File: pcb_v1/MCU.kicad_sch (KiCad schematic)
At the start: 3 parts, among them U4 ESP32-S3-MINI-1, U6 STM32F103RETx

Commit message: Updated wiring
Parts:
- C12: footprint Capacitor_SMD:C_0805_2012Metric -> Murata Capacitor:CAPC1608X90N
- U4: footprint RF_Module:ESP32-S2-MINI-1 -> ESP32-S3-MINI-1-N8:XCVR_ESP32-S3-MINI-1-N8
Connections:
- net +3.3V: now also U4.3 (3V3)
- net D+: now also U6.45 (PA12)
- net D-: now also U6.44 (PA11)
- net GND: now also U4.1 (GND), U4.2 (GND), U4.42 (GND), U4.43 (GND), U4.46 (GND), U4.47 (GND), U4.48 (GND), U4.49 (GND), U4.50 (GND), U4.51 (GND), U4.52 (GND), U4.53 (GND), U4.54 (GND), U4.55 (GND), U4.56 (GND), U4.57 (GND), U4.58 (GND), U4.59 (GND), U4.60 (GND), U4.61 (GND), U4.62 (GND), U4.63 (GND), U4.64 (GND), U4.65 (GND)
- net SCL: now also U6.58 (PB6)
- net SDA: now also U6.59 (PB7)
- net TXRX: now reaches U6.42 (PA9)
- net TXRX: now also U4.40 (RXD0)
- net RXTX: now reaches U6.43 (PA10)
- net RXTX: now also U4.39 (TXD0)
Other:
- moved on the sheet: C12, U4, U6

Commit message: Update Wiring
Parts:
- removed C12: 100nF, Murata Capacitor:CAPC1608X90N, symbol Device:C
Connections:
- net Column11: now also U6.54 (PD2)
- net Column12: now also U6.55 (PB3)
- net Column13: now also U6.56 (PB4)
- net Column14: now also U6.57 (PB5)
- net Column3: now also U6.25 (PC5)
- net Column4: now also U6.26 (PB0)
- net Column5: now also U6.27 (PB1)
- net Column6: now also U6.28 (PB2)
- net Column7: now also U6.29 (PB10)
- net Column8: now also U6.30 (PB11)
- net RDY: now also U6.61 (PB8)
- net NRST: now reaches U6.7 (NRST)

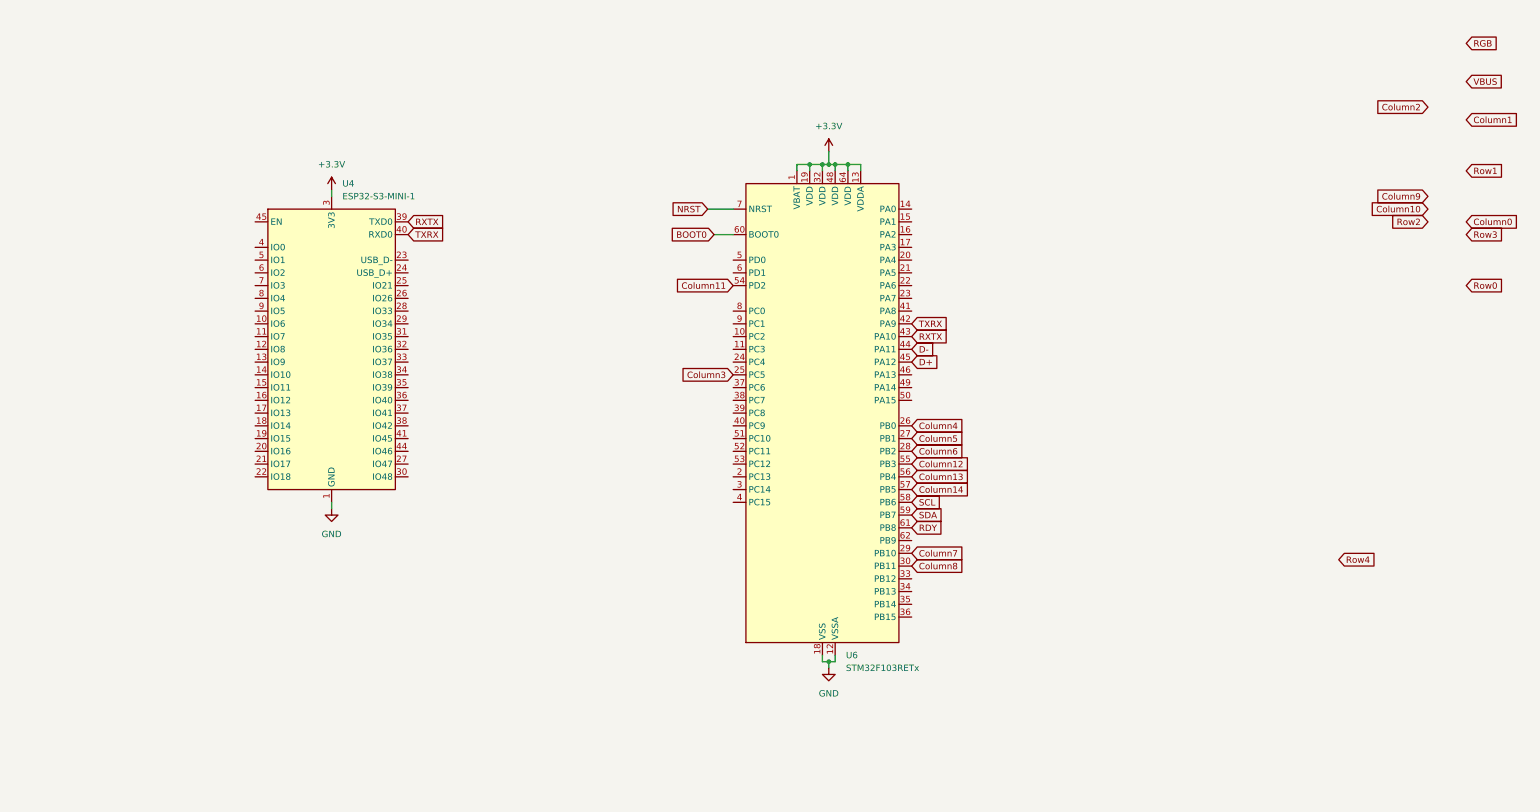
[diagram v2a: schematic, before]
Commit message: Wired all keyboard matrix pins
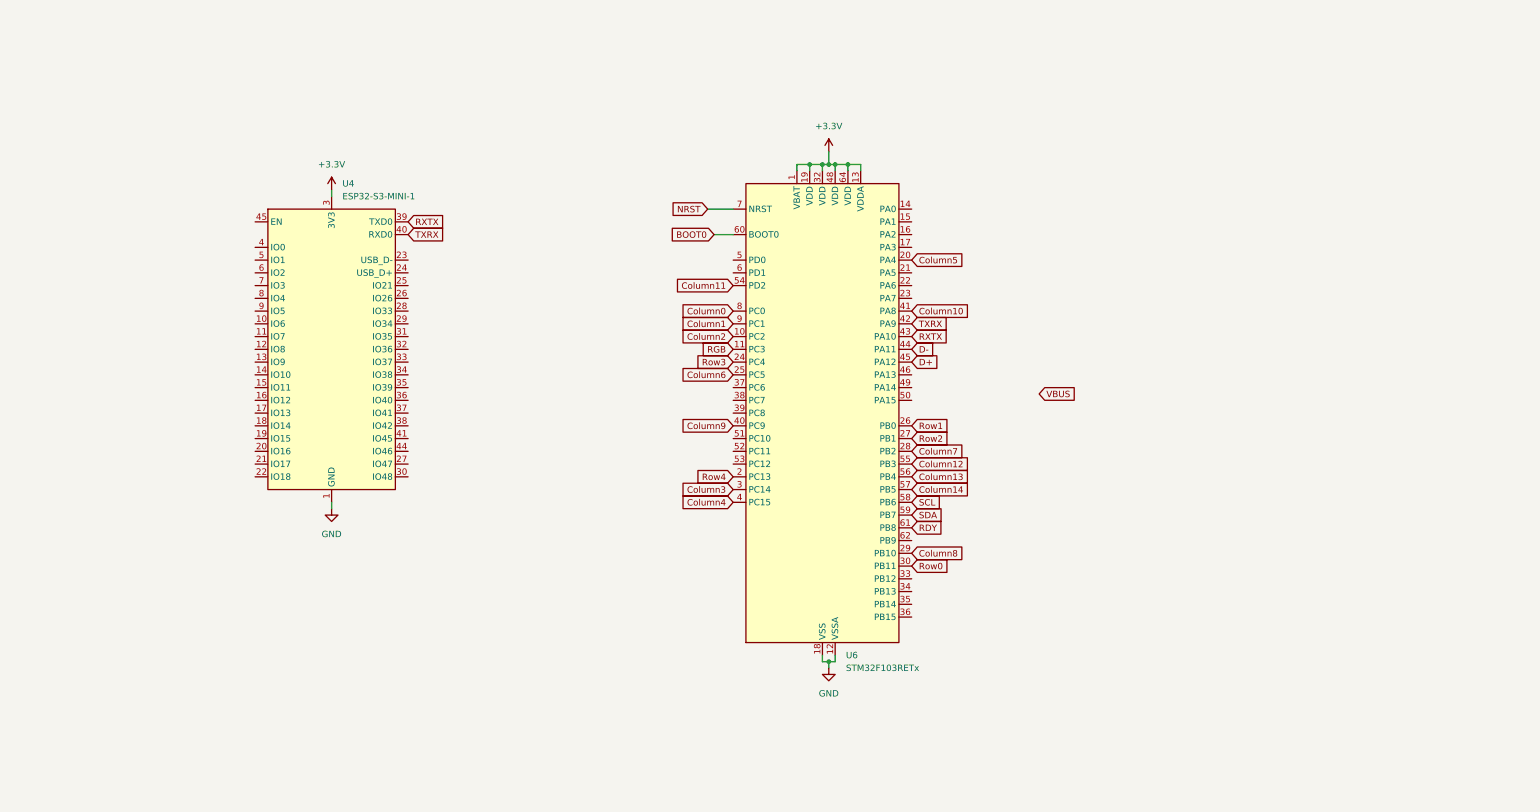
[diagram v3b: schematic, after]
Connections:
- net Column0: now also U6.8 (PC0)
- net Column1: now also U6.9 (PC1)
- net Column10: now also U6.41 (PA8)
- net Column2: now also U6.10 (PC2)
- net Column3: now also U6.3 (PC14); no longer U6.25 (PC5)
- net Column4: now also U6.4 (PC15); no longer U6.26 (PB0)
- net Column5: now also U6.20 (PA4); no longer U6.27 (PB1)
- net Column6: now also U6.25 (PC5); no longer U6.28 (PB2)
- net Column7: now also U6.28 (PB2); no longer U6.29 (PB10)
- net Column8: now also U6.29 (PB10); no longer U6.30 (PB11)
- net Column9: now also U6.40 (PC9)
- net RGB: now also U6.11 (PC3)
- net Row0: now also U6.30 (PB11)
- net Row1: now also U6.26 (PB0)
- net Row2: now also U6.27 (PB1)
- net Row3: now also U6.24 (PC4)
- net Row4: now also U6.2 (PC13)

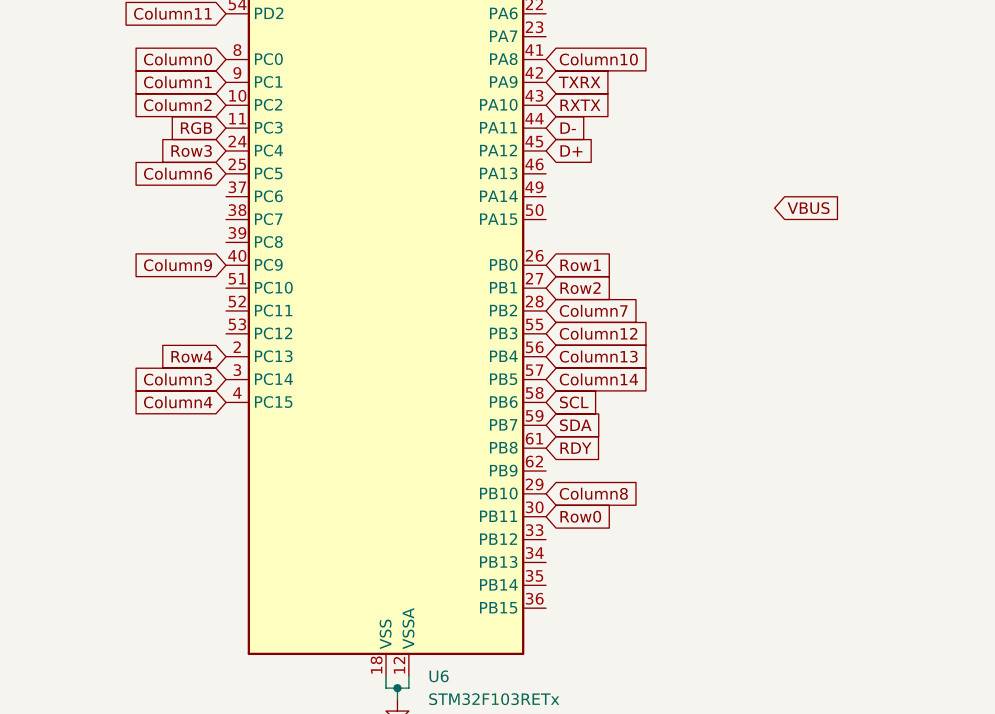
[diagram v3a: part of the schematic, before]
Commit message: Connected OLED pin connector
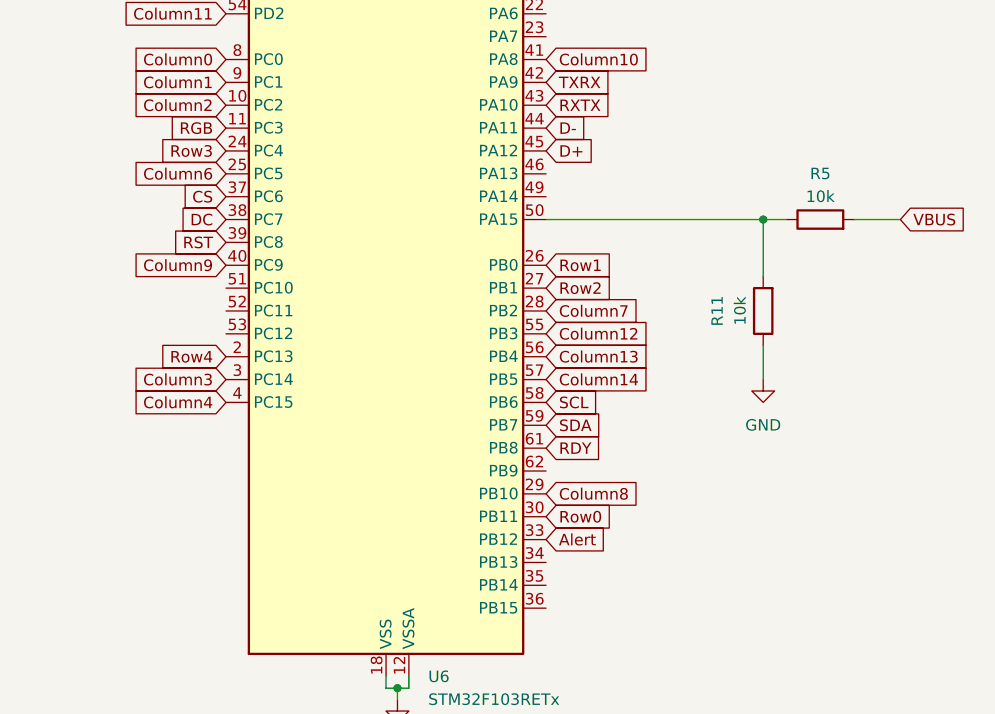
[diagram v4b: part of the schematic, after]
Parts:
- added R11, R5: 10k, RC0402FR-7D4K7L:RESC1005X40N, symbol ScottoKeebs:Placeholder_Resistor
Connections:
- net GND: now also R11.1
- net VBUS: now also R5.2
- net Alert: now reaches U6.33 (PB12)
- net CS: now reaches U6.37 (PC6)
- net DC: now reaches U6.38 (PC7)
- net RST: now reaches U6.39 (PC8)
- net at U6.50 (PA15): now also R11.2, R5.1

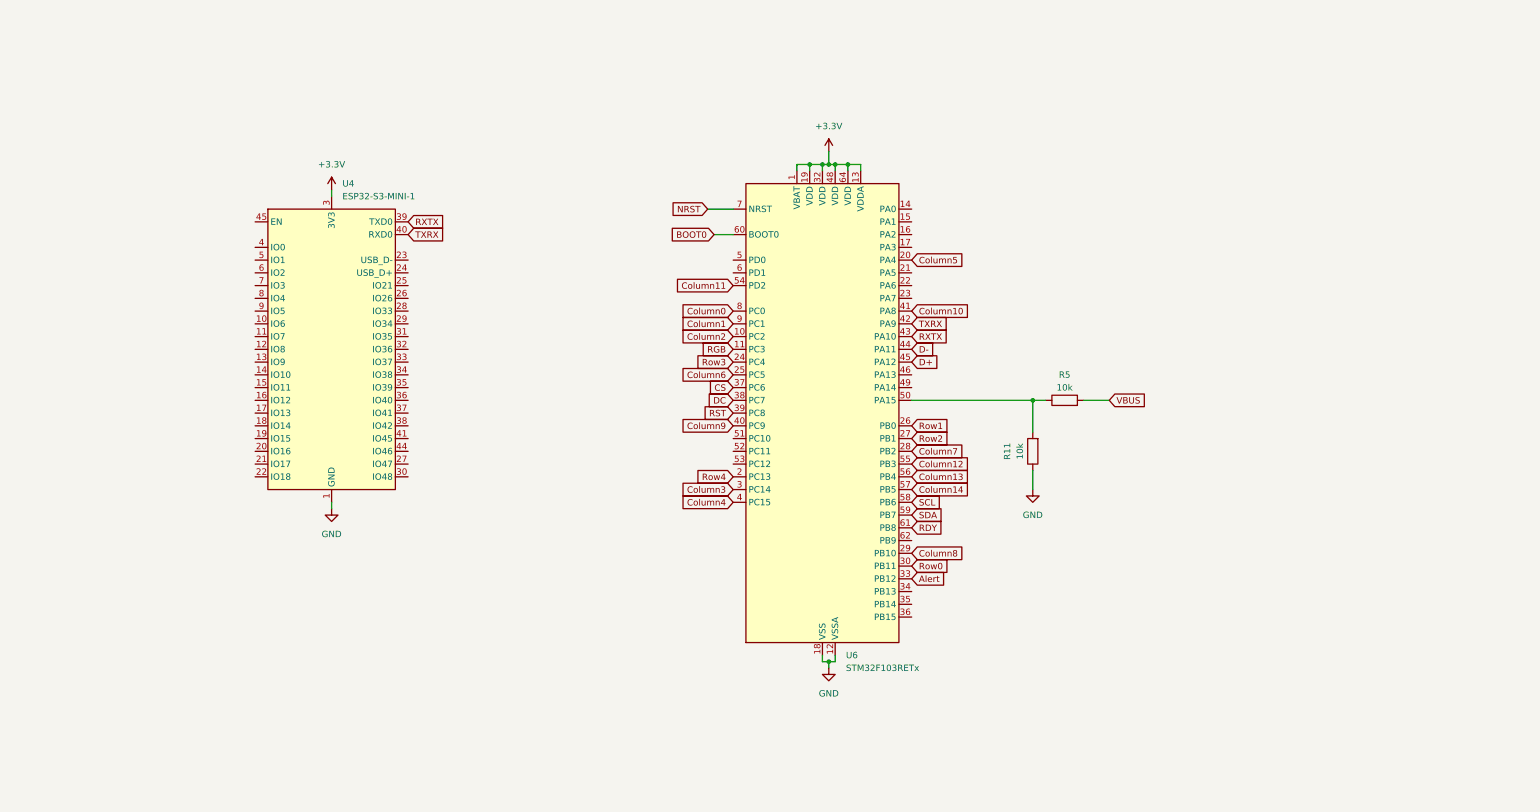
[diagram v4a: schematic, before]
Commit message: Changed Layout of Keyboard
Row 1, Column 14 Removed due to OLED Screen taking up 2x2 u space
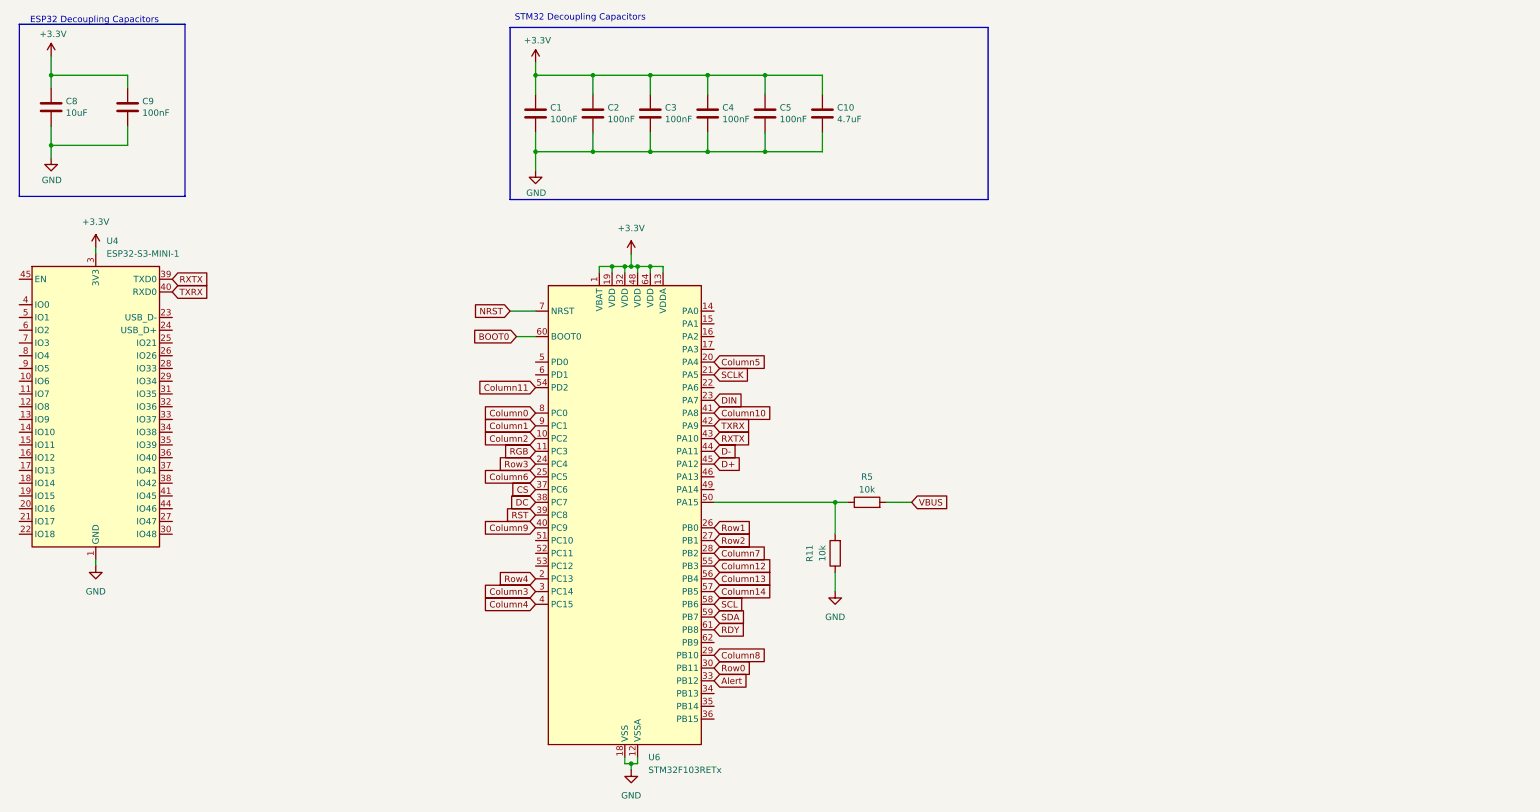
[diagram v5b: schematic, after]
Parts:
- added C1, C2, C3, C4, C5, C9: 100nF, GRM1555C2A101GA01D:CAPC1005X55N, symbol Device:C
- added C10: 4.7uF, GRM1555C2A101GA01D:CAPC1005X55N, symbol Device:C
- added C8: 10uF, GRM1555C2A101GA01D:CAPC1005X55N, symbol Device:C
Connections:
- net +3.3V: now also C1.1, C10.1, C2.1, C3.1, C4.1, C5.1, C8.1, C9.1
- net GND: now also C1.2, C10.2, C2.2, C3.2, C4.2, C5.2, C8.2, C9.2
- net SCLK: now reaches U6.21 (PA5)
- net DIN: now reaches U6.23 (PA7)
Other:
- note added: "ESP32 Decoupling Capacitors"
- note added: "STM32 Decoupling Capacitors"
- moved on the sheet: R11, R5, U4, U6

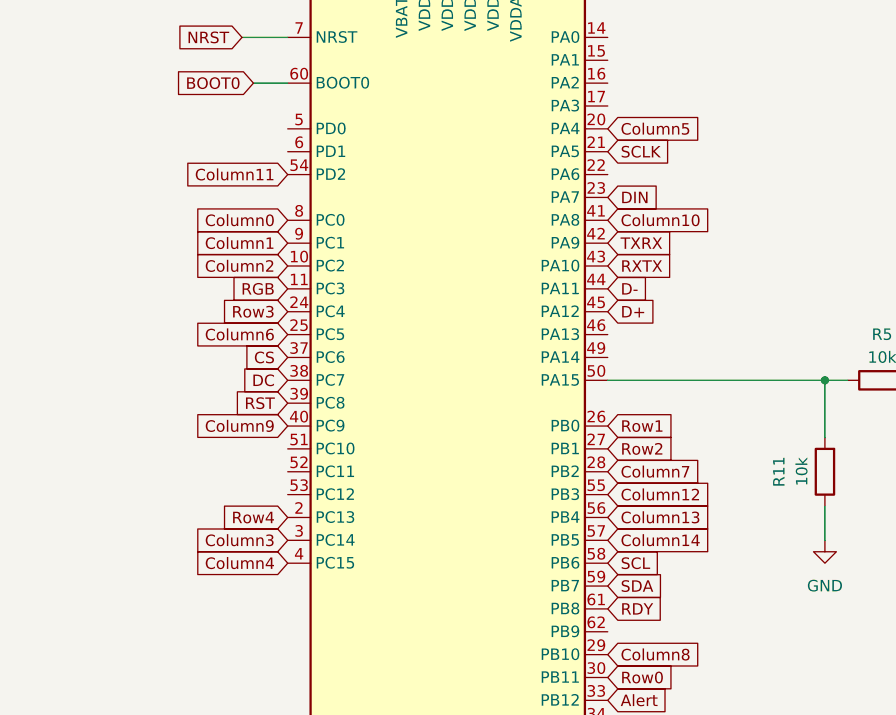
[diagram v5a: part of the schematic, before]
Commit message: Changed PCB to Accommodate Revised Layout
Added a few more keys to balance the screen being 2u x 2u, therefore extending the length of the PCB
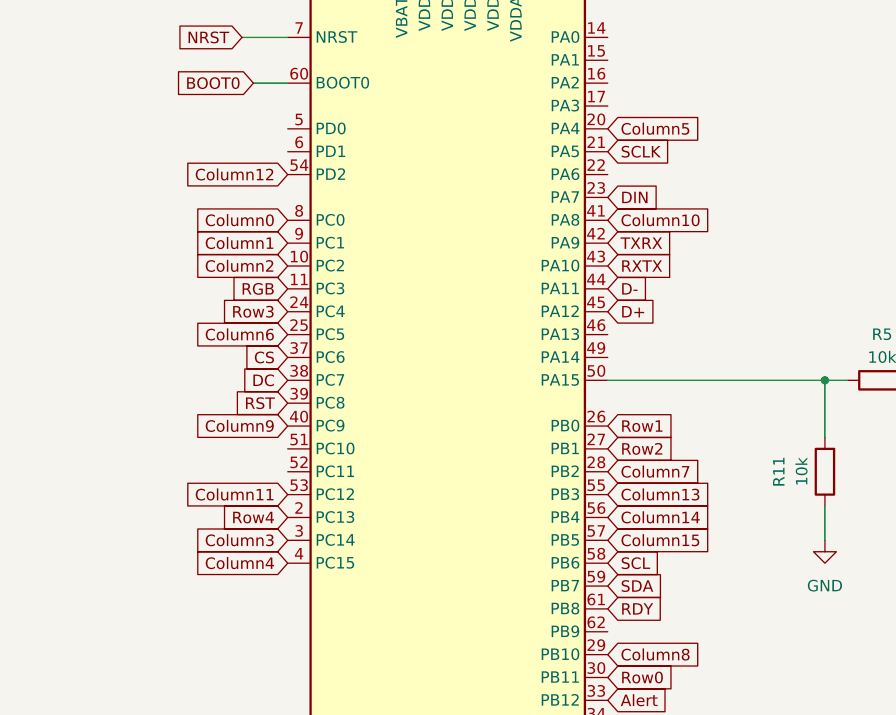
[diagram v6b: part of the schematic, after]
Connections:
- net Column11: now also U6.53 (PC12); no longer U6.54 (PD2)
- net Column12: now also U6.54 (PD2); no longer U6.55 (PB3)
- net Column13: now also U6.55 (PB3); no longer U6.56 (PB4)
- net Column14: now also U6.56 (PB4); no longer U6.57 (PB5)
- new net Column15: U6.57 (PB5)
